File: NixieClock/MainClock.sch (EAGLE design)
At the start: 20 parts, among them IC1 MEGA8-P

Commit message: Finished first sheet. Declares the 5V as VCC and began second sheet.
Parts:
- added ANODE: (no value), con-lsta:FE06-1
- added CATHODE: (no value), con-lsta:FE10-1
- added R20, R21, R22, R23, R24, R26: 15k, resistor:R-EU_0309/10
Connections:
- new net N$11: ANODE.6, R26.1
- new net N$12: ANODE.5, R23.1
- new net N$13: ANODE.4, R24.1
- new net N$14: ANODE.3, R22.1
- new net N$15: ANODE.2, R21.1
- new net N$16: ANODE.1, R20.1
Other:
- note added: "Note: Numbering of these Resistors is a bit Strange. But I keep it to avoid confusion"
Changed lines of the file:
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@@
 <setting verticaltext="up"/>
 </settings>
-<grid distance="0.1" unitdist="inch" unit="inch" style="lines" multiple="1" display="no" altdistance="0.01" altunitdist="inch" altunit="inch"/>
+<grid distance="1" unitdist="mm" unit="mm" style="dots" multiple="1" display="yes" altdistance="0.1" altunitdist="mm" altunit="mm"/>
 <layers>
 <layer number="1" name="Top" color="4" fill="1" visible="no" active="no"/>
@@
 <part name="R35" library="resistor" library_urn="urn:adsk.eagle:library:348" deviceset="R-EU_" device="0309/10" package3d_urn="urn:adsk.eagle:package:26087/1" value="1k"/>
 <part name="POWER_LED" library="led" library_urn="urn:adsk.eagle:library:259" deviceset="LED" device="5MM" package3d_urn="urn:adsk.eagle:package:15799/2"/>
+<part name="ANODE" library="con-lsta" library_urn="urn:adsk.eagle:library:161" deviceset="FE06-1" device="" package3d_urn="urn:adsk.eagle:package:8191/1"/>
+<part name="CATHODE" library="con-lsta" library_urn="urn:adsk.eagle:library:161" deviceset="FE10-1" device="" package3d_urn="urn:adsk.eagle:package:8192/1"/>
+<part name="P+1" library="supply1" library_urn="urn:adsk.eagle:library:371" deviceset="VCC" device=""/>
+<part name="R26" library="resistor" library_urn="urn:adsk.eagle:library:348" deviceset="R-EU_" device="0309/10" package3d_urn="urn:adsk.eagle:package:26087/1" value="15k"/>
+<part name="R21" library="resistor" library_urn="urn:adsk.eagle:library:348" deviceset="R-EU_" device="0309/10" package3d_urn="urn:adsk.eagle:package:26087/1" value="15k"/>
+<part name="R22" library="resistor" library_urn="urn:adsk.eagle:library:348" deviceset="R-EU_" device="0309/10" package3d_urn="urn:adsk.eagle:package:26087/1" value="15k"/>
+<part name="R20" library="resistor" library_urn="urn:adsk.eagle:library:348" deviceset="R-EU_" device="0309/10" package3d_urn="urn:adsk.eagle:package:26087/1" value="15k"/>
+<part name="R23" library="resistor" library_urn="urn:adsk.eagle:library:348" deviceset="R-EU_" device="0309/10" package3d_urn="urn:adsk.eagle:package:26087/1" value="15k"/>
+<part name="R24" library="resistor" library_urn="urn:adsk.eagle:library:348" deviceset="R-EU_" device="0309/10" package3d_urn="urn:adsk.eagle:package:26087/1" value="15k"/>
 </parts>
 <sheets>
@@
 <instance part="R35" gate="G$1" x="-58.42" y="119.38"/>
 <instance part="POWER_LED" gate="G$1" x="-48.26" y="175.26"/>
+<instance part="P+1" gate="VCC" x="-77" y="193" rot="R90"/>
 </instances>
 <busses>
@@
 <pinref part="C7" gate="G$1" pin="+"/>
 <wire x1="-20.32" y1="193.04" x2="-66.04" y2="193.04" width="0.1524" layer="91"/>
-<wire x1="-66.04" y1="193.04" x2="-73.66" y2="193.04" width="0.1524" layer="91"/>
 <wire x1="-20.32" y1="200.66" x2="-20.32" y2="193.04" width="0.1524" layer="91"/>
 <junction x="-20.32" y="193.04"/>
 <wire x1="-66.04" y1="193.04" x2="-66.04" y2="185.42" width="0.1524" layer="91"/>
-<junction x="-66.04" y="193.04"/>
 <pinref part="R27" gate="G$1" pin="1"/>
 <wire x1="-66.04" y1="185.42" x2="-63.5" y2="185.42" width="0.1524" layer="91"/>
@@
 </segment>
 </net>
+<net name="VCC" class="0">
+<segment>
+<pinref part="P+1" gate="VCC" pin="VCC"/>
+<wire x1="-66" y1="193" x2="-74.46" y2="193" width="0.1524" layer="91"/>
+</segment>
+</net>
+</nets>
+</sheet>
+<sheet>
+<plain>
+<text x="15" y="72" size="1.778" layer="91">Note:
+Numbering of these Resistors is a bit Strange.
+But I keep it to avoid confusion</text>
+</plain>
+<instances>
+<instance part="ANODE" gate="G$1" x="14" y="54"/>
+<instance part="CATHODE" gate="G$1" x="40" y="103"/>
+<instance part="R26" gate="G$1" x="39.58" y="65.38" smashed="yes">
+<attribute name="NAME" x="35.77" y="66.8786" size="1.778" layer="95"/>
+</instance>
+<instance part="R21" gate="G$1" x="39.58" y="49.38" smashed="yes">
+<attribute name="NAME" x="35.77" y="50.8786" size="1.778" layer="95"/>
+</instance>
+<instance part="R22" gate="G$1" x="39.58" y="53.38" smashed="yes">
+<attribute name="NAME" x="35.77" y="54.8786" size="1.778" layer="95"/>
+</instance>
+<instance part="R20" gate="G$1" x="39.58" y="45.38" smashed="yes">
+<attribute name="NAME" x="35.77" y="46.8786" size="1.778" layer="95"/>
+</instance>
+<instance part="R23" gate="G$1" x="39.58" y="61.38" smashed="yes">
+<attribute name="NAME" x="35.77" y="62.8786" size="1.778" layer="95"/>
+</instance>
+<instance part="R24" gate="G$1" x="39.58" y="57.38" smashed="yes">
+<attribute name="NAME" x="35.77" y="58.8786" size="1.778" layer="95"/>
+</instance>
+</instances>
+<busses>
+</busses>
+<nets>
+<net name="N$11" class="0">
+<segment>
+<pinref part="ANODE" gate="G$1" pin="6"/>
+<pinref part="R26" gate="G$1" pin="1"/>
+<wire x1="21.62" y1="61.62" x2="21.62" y2="65.38" width="0.1524" layer="91"/>
+<wire x1="21.62" y1="65.38" x2="34.5" y2="65.38" width="0.1524" layer="91"/>
+</segment>
+</net>
+<net name="N$12" class="0">
+<segment>
+<pinref part="ANODE" gate="G$1" pin="5"/>
+<pinref part="R23" gate="G$1" pin="1"/>
+<wire x1="21.62" y1="59.08" x2="34.5" y2="59.08" width="0.1524" layer="91"/>
+<wire x1="34.5" y1="59.08" x2="34.5" y2="61.38" width="0.1524" layer="91"/>
+</segment>
+</net>
+<net name="N$13" class="0">
+<segment>
+<pinref part="ANODE" gate="G$1" pin="4"/>
+<pinref part="R24" gate="G$1" pin="1"/>
+<wire x1="21.62" y1="56.54" x2="34.5" y2="56.54" width="0.1524" layer="91"/>
+<wire x1="34.5" y1="56.54" x2="34.5" y2="57.38" width="0.1524" layer="91"/>
+</segment>
+</net>
+<net name="N$14" class="0">
+<segment>
+<pinref part="ANODE" gate="G$1" pin="3"/>
+<pinref part="R22" gate="G$1" pin="1"/>
+<wire x1="21.62" y1="54" x2="34.5" y2="54" width="0.1524" layer="91"/>
+<wire x1="34.5" y1="54" x2="34.5" y2="53.38" width="0.1524" layer="91"/>
+</segment>
+</net>
+<net name="N$15" class="0">
+<segment>
+<pinref part="ANODE" gate="G$1" pin="2"/>
+<pinref part="R21" gate="G$1" pin="1"/>
+<wire x1="21.62" y1="51.46" x2="34.5" y2="51.46" width="0.1524" layer="91"/>
+<wire x1="34.5" y1="51.46" x2="34.5" y2="49.38" width="0.1524" layer="91"/>
+</segment>
+</net>
+<net name="N$16" class="0">
+<segment>
+<pinref part="ANODE" gate="G$1" pin="1"/>
+<pinref part="R20" gate="G$1" pin="1"/>
+<wire x1="21.62" y1="48.92" x2="34.5" y2="48.92" width="0.1524" layer="91"/>
+<wire x1="34.5" y1="48.92" x2="34.5" y2="45.38" width="0.1524" layer="91"/>
+</segment>
+</net>
 </nets>
 </sheet>
@@
 </drawing>
 <compatibility>
+<note version="6.3" minversion="6.2.2" severity="warning">
+Since Version 6.2.2 text objects can contain more than one line,
+which will not be processed correctly with this version.
+</note>
 <note version="8.2" severity="warning">
 Since Version 8.2, EAGLE supports online libraries. The ids

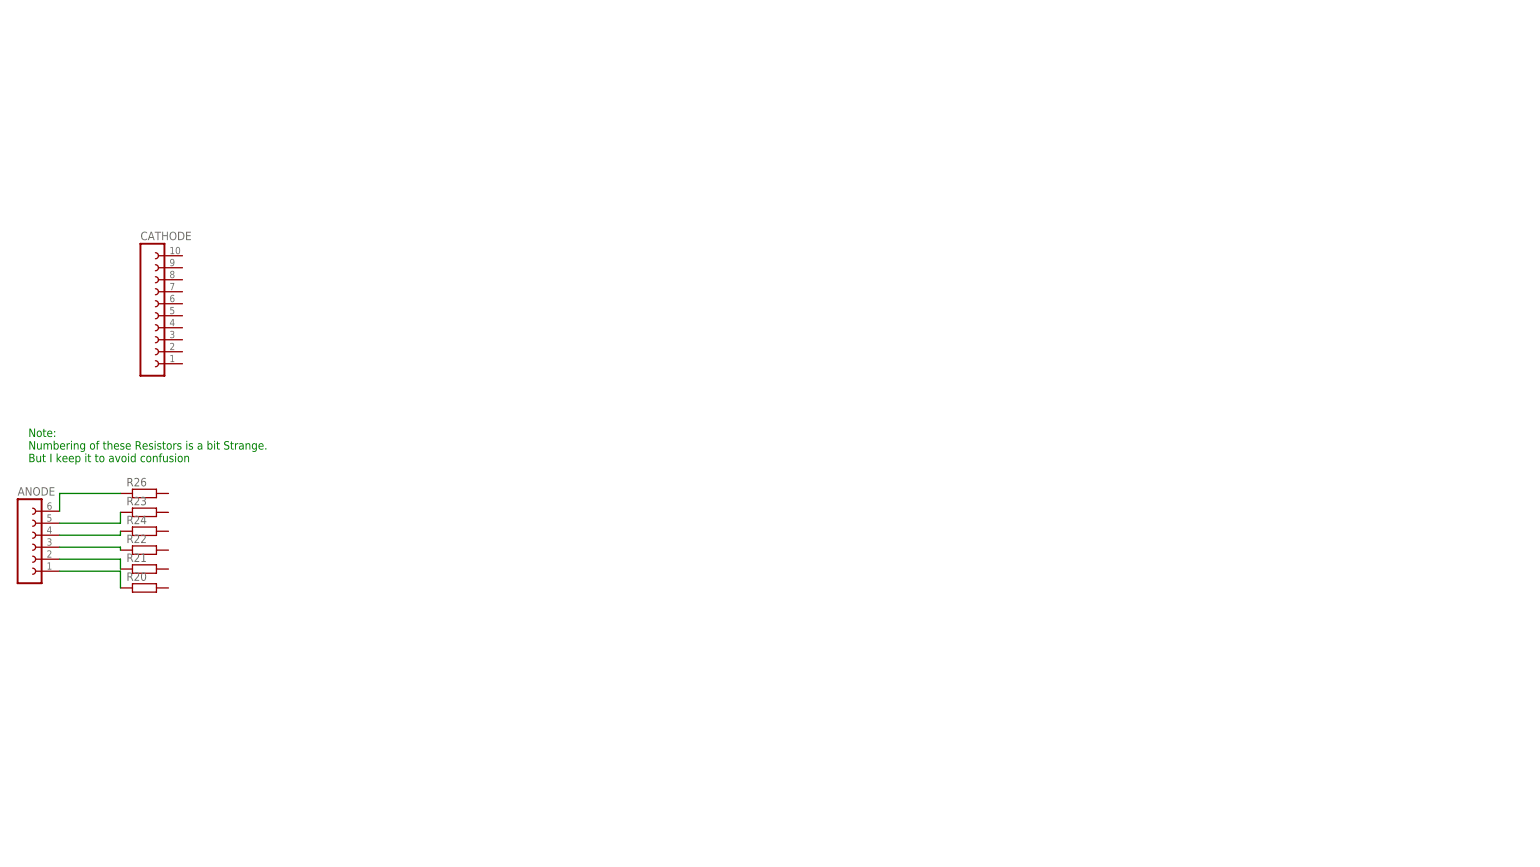
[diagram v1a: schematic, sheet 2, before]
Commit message: Completed Section A of Sheet 2
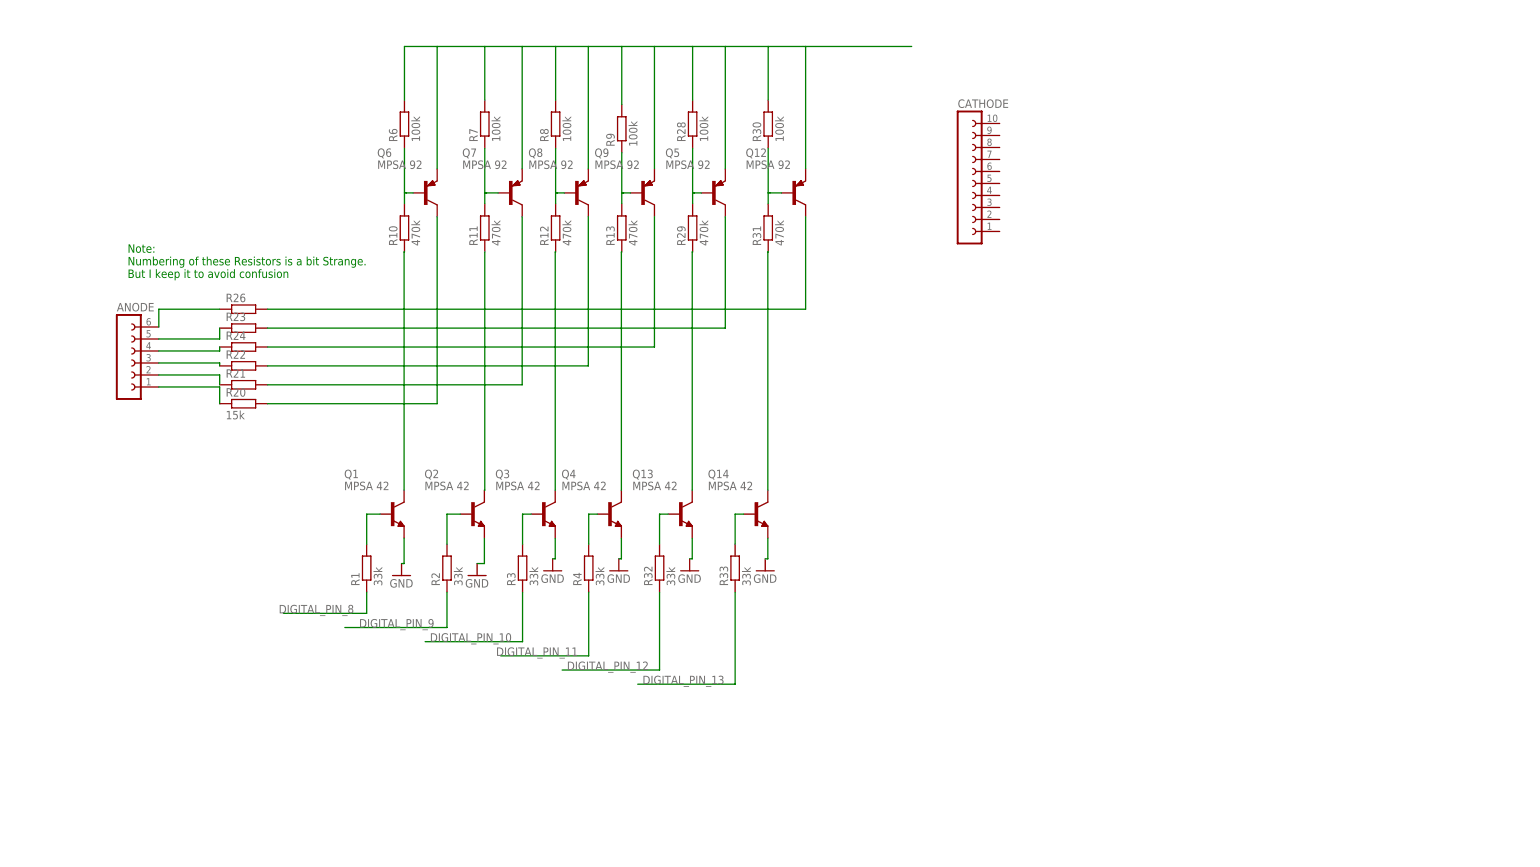
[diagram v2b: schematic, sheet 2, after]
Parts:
- added Q1, Q13, Q14, Q2, Q3, Q4: MPSA 42, transistor:-NPN-TO92
- added Q12, Q5, Q6, Q7, Q8, Q9: MPSA 92, transistor:MPSA92-PNP-TO92-EBC
- added R1, R2, R3, R32, R33, R4: 33k, resistor:R-EU_0309/10
- added R10, R11, R12, R13, R29, R31: 470k, resistor:R-EU_0309/10
- added R28, R30, R6, R7, R8, R9: 100k, resistor:R-EU_0309/10
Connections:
- new net N$17: Q1.B, R1.2
- new net N$18: Q2.B, R2.2
- new net N$19: Q13.B, R32.2
- new net N$20: Q14.B, R33.2
- new net N$21: Q4.B, R4.2
- new net N$22: Q3.B, R3.2
- new net N$23: Q1.C, R10.1
- new net N$24: Q2.C, R11.1
- new net N$25: Q3.C, R12.1
- new net N$26: Q4.C, R13.1
- new net N$27: Q13.C, R29.1
- new net N$28: Q14.C, R31.1
- new net N$29: Q12.B, R30.1, R31.2
- new net N$30: Q5.B, R28.1, R29.2
- new net N$31: Q9.B, R13.2, R9.1
- new net N$32: Q8.B, R12.2, R8.1
- new net N$33: Q7.B, R11.2, R7.1
- new net N$34: Q6.B, R10.2, R6.1
- new net N$35: Q12.C, R26.2
- new net N$36: Q5.C, R23.2
- new net N$37: Q9.C, R24.2
- new net N$38: Q8.C, R22.2
- new net N$39: Q7.C, R21.2
- new net N$40: Q6.C, R20.2
- new net N$41: Q12.E, Q5.E, Q6.E, Q7.E, Q8.E, Q9.E, R28.2, R30.2, R6.2, R7.2, R8.2, R9.2
- net DIGITAL_PIN_10: now also R3.1
- net DIGITAL_PIN_11: now also R4.1
- net DIGITAL_PIN_12: now also R32.1
- net DIGITAL_PIN_13: now also R33.1
- net DIGITAL_PIN_8: now also R1.1
- net DIGITAL_PIN_9: now also R2.1
- net GND: now also Q1.E, Q13.E, Q14.E, Q2.E, Q3.E, Q4.E
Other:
- moved on the sheet: ANODE, CATHODE, R20, R21, R22, R23, R24, R26

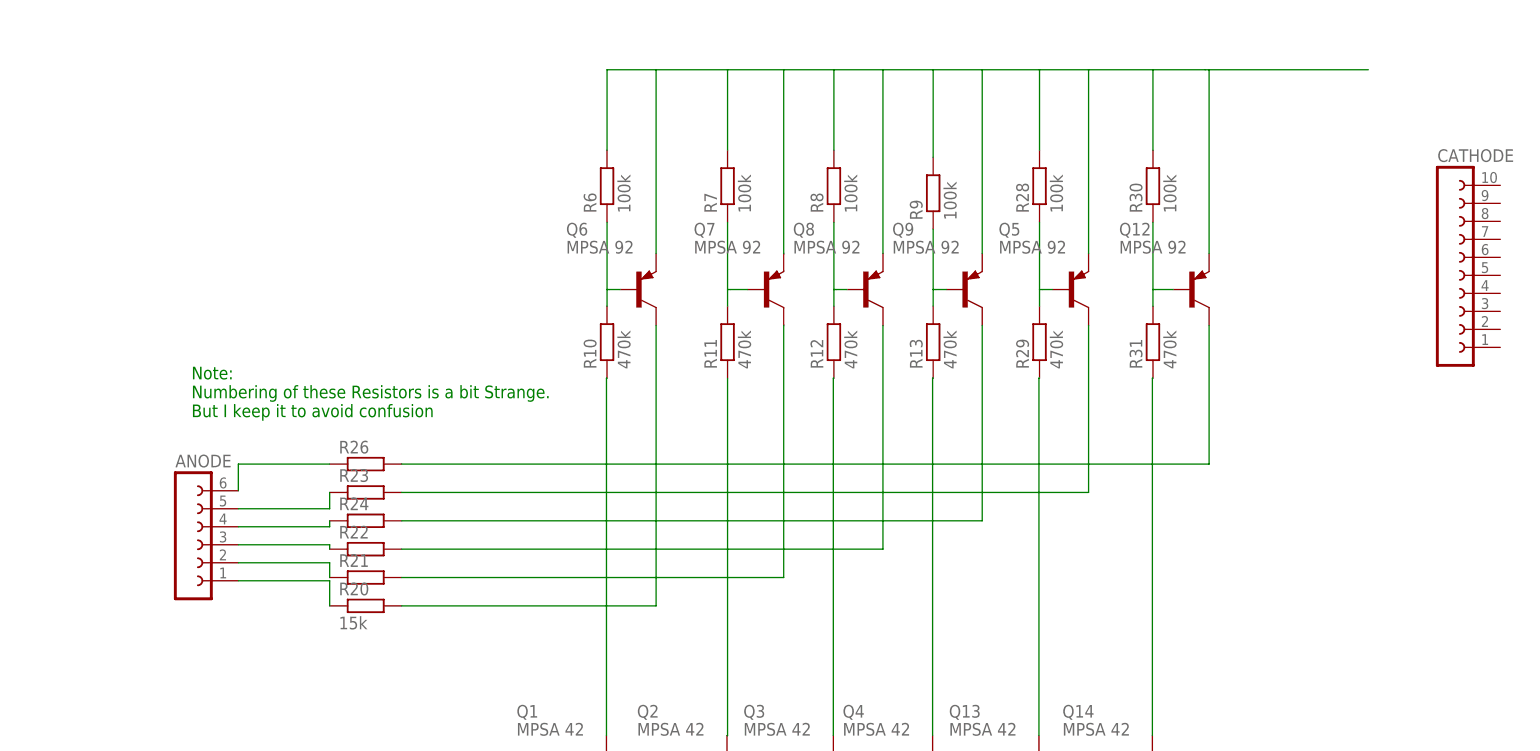
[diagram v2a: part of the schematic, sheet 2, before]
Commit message: Completed Section B of Sheet 2 and exchanged female heades with pins.
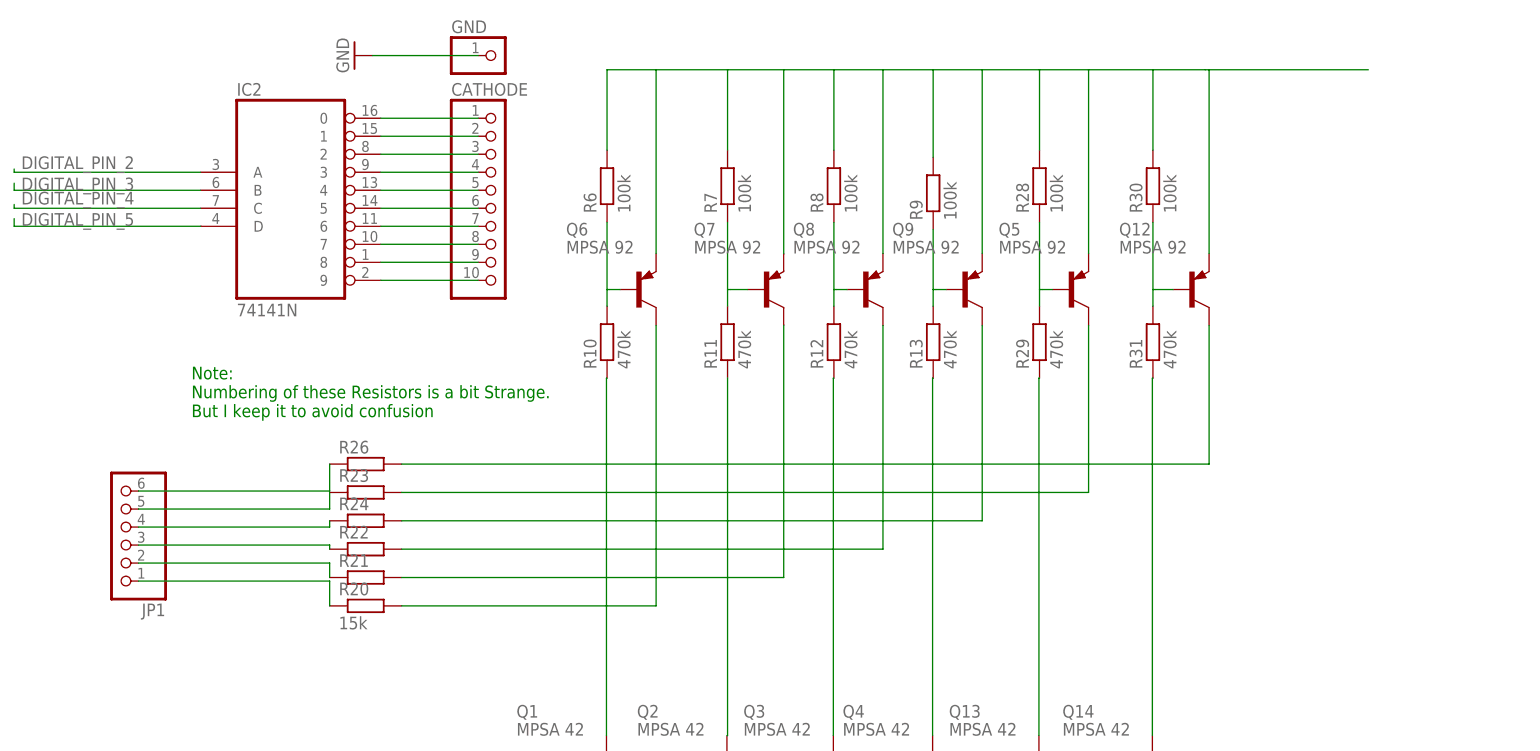
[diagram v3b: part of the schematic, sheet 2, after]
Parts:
- removed ANODE: (no value), con-lsta:FE06-1
- added GND: (no value), pinhead:PINHD-1X1
- added IC2: 74141N, 74xx-us:74141N
- added JP1: (no value), pinhead:PINHD-1X6
- CATHODE: device con-lsta:FE10-1 -> pinhead:PINHD-1X10
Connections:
- new net N$42: CATHODE.1, IC2A.0
- new net N$43: CATHODE.2, IC2A.1
- new net N$44: CATHODE.6, IC2A.5
- new net N$45: CATHODE.5, IC2A.4
- new net N$46: CATHODE.7, IC2A.6
- new net N$47: CATHODE.8, IC2A.7
- new net N$48: CATHODE.4, IC2A.3
- new net N$49: CATHODE.3, IC2A.2
- new net N$50: CATHODE.9, IC2A.8
- new net N$51: CATHODE.10, IC2A.9
- net DIGITAL_PIN_2: now also IC2A.A
- net DIGITAL_PIN_3: now also IC2A.B
- net DIGITAL_PIN_4: now also IC2A.C
- net DIGITAL_PIN_5: now also IC2A.D
- net GND: now also GND.1
- net N$11: now also JP1.6; no longer ANODE.6
- net N$12: now also JP1.5; no longer ANODE.5
- net N$13: now also JP1.4; no longer ANODE.4
- net N$14: now also JP1.3; no longer ANODE.3
- net N$15: now also JP1.2; no longer ANODE.2
- net N$16: now also JP1.1; no longer ANODE.1
